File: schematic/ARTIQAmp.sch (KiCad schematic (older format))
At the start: 9 parts, among them J1 Power conneciton, J2 HD68, J3 HD68

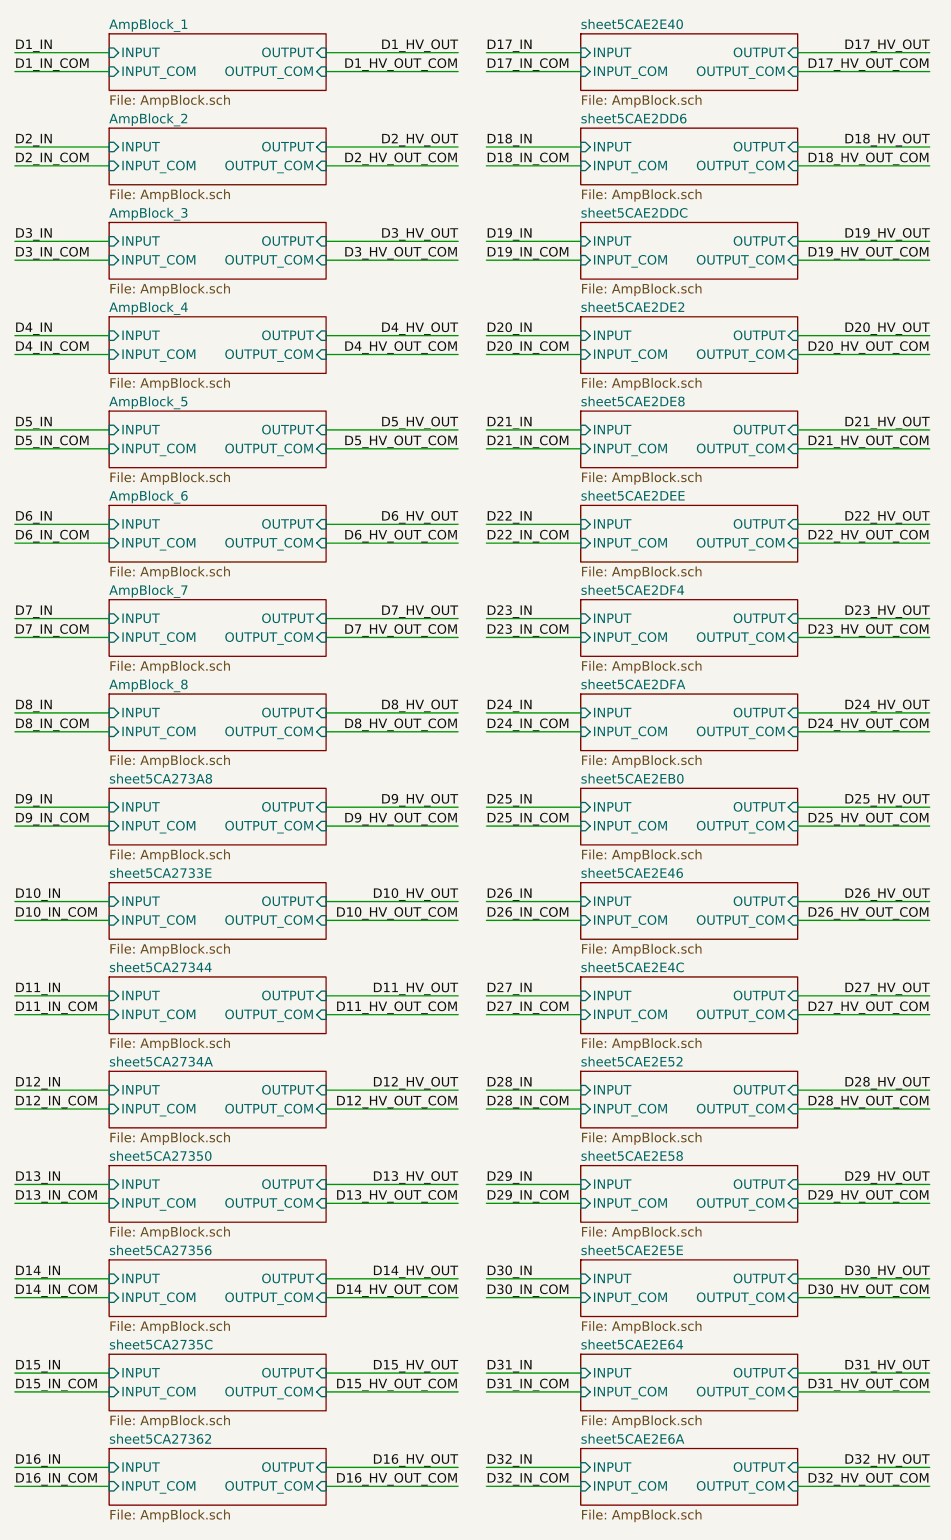
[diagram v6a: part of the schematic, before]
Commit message: Updating with recent changes as layout work starts
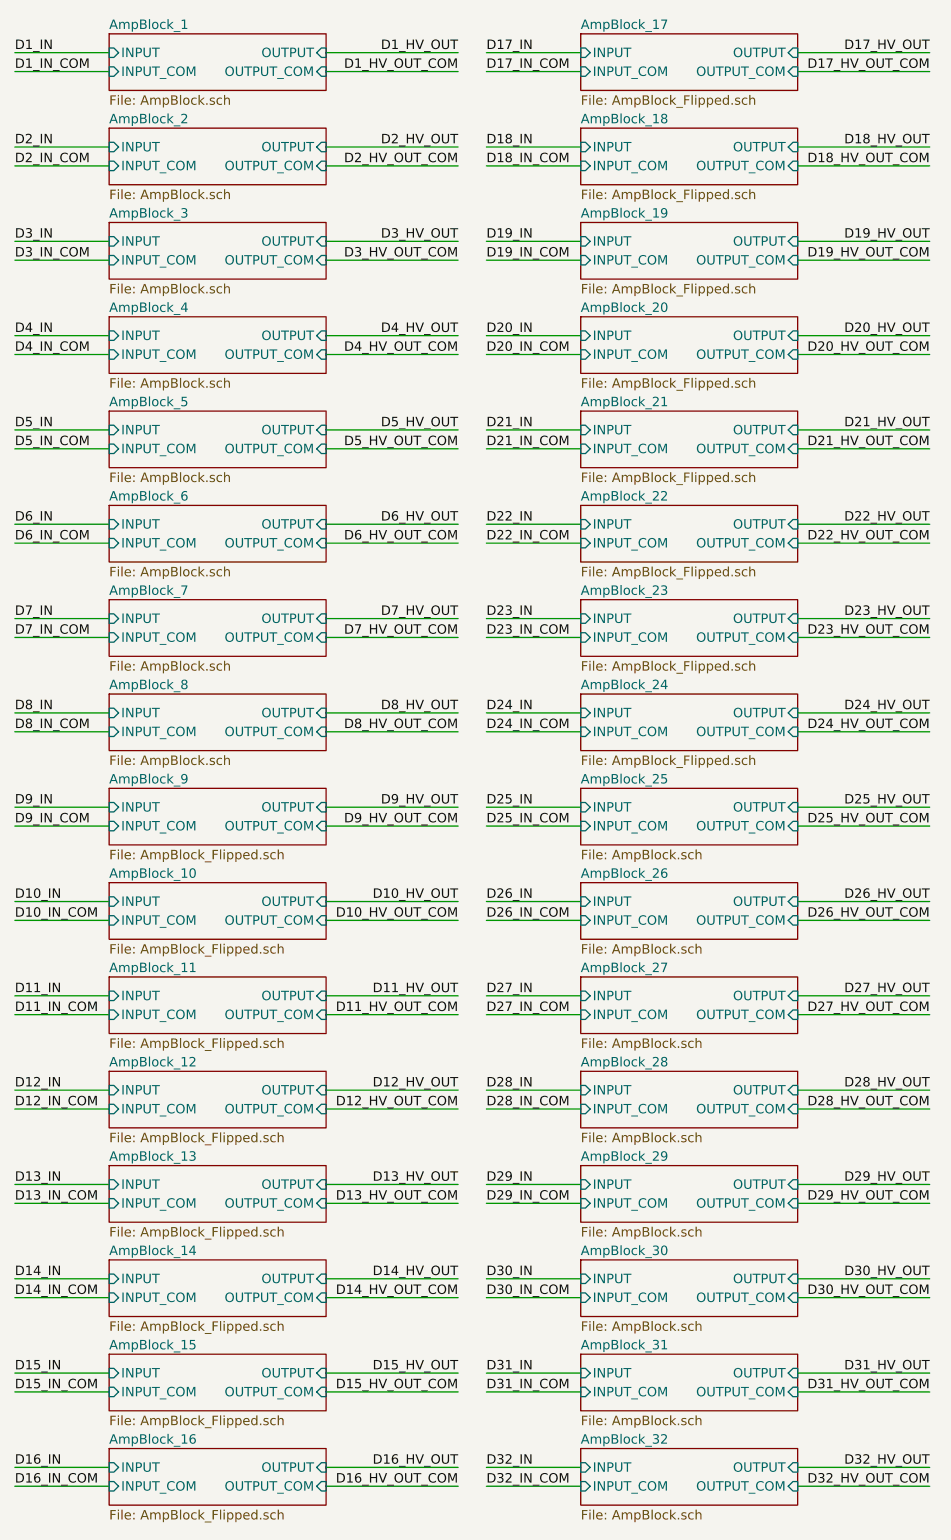
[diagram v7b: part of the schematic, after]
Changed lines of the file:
@@
 S 1150 5400 1150 300
 U 5CA2733E
-F0 "sheet5CA2733E" 50
-F1 "AmpBlock.sch" 50
+F0 "AmpBlock_10" 50
+F1 "AmpBlock_Flipped.sch" 50
 F2 "INPUT" I L 1150 5500 50
 F3 "OUTPUT" I R 2300 5500 50
@@
 S 1150 5900 1150 300
 U 5CA27344
-F0 "sheet5CA27344" 50
-F1 "AmpBlock.sch" 50
+F0 "AmpBlock_11" 50
+F1 "AmpBlock_Flipped.sch" 50
 F2 "INPUT" I L 1150 6000 50
 F3 "OUTPUT" I R 2300 6000 50
@@
 S 1150 6400 1150 300
 U 5CA2734A
-F0 "sheet5CA2734A" 50
-F1 "AmpBlock.sch" 50
+F0 "AmpBlock_12" 50
+F1 "AmpBlock_Flipped.sch" 50
 F2 "INPUT" I L 1150 6500 50
 F3 "OUTPUT" I R 2300 6500 50
@@
 S 1150 6900 1150 300
 U 5CA27350
-F0 "sheet5CA27350" 50
-F1 "AmpBlock.sch" 50
+F0 "AmpBlock_13" 50
+F1 "AmpBlock_Flipped.sch" 50
 F2 "INPUT" I L 1150 7000 50
 F3 "OUTPUT" I R 2300 7000 50
@@
 S 1150 7400 1150 300
 U 5CA27356
-F0 "sheet5CA27356" 50
-F1 "AmpBlock.sch" 50
+F0 "AmpBlock_14" 50
+F1 "AmpBlock_Flipped.sch" 50
 F2 "INPUT" I L 1150 7500 50
 F3 "OUTPUT" I R 2300 7500 50
@@
 S 1150 7900 1150 300
 U 5CA2735C
-F0 "sheet5CA2735C" 50
-F1 "AmpBlock.sch" 50
+F0 "AmpBlock_15" 50
+F1 "AmpBlock_Flipped.sch" 50
 F2 "INPUT" I L 1150 8000 50
 F3 "OUTPUT" I R 2300 8000 50
@@
 S 1150 8400 1150 300
 U 5CA27362
-F0 "sheet5CA27362" 50
-F1 "AmpBlock.sch" 50
+F0 "AmpBlock_16" 50
+F1 "AmpBlock_Flipped.sch" 50
 F2 "INPUT" I L 1150 8500 50
 F3 "OUTPUT" I R 2300 8500 50
@@
 S 1150 4900 1150 300
 U 5CA273A8
-F0 "sheet5CA273A8" 50
-F1 "AmpBlock.sch" 50
+F0 "AmpBlock_9" 50
+F1 "AmpBlock_Flipped.sch" 50
 F2 "INPUT" I L 1150 5000 50
 F3 "OUTPUT" I R 2300 5000 50
@@
 S 3650 1400 1150 300
 U 5CAE2DD6
-F0 "sheet5CAE2DD6" 50
-F1 "AmpBlock.sch" 50
+F0 "AmpBlock_18" 50
+F1 "AmpBlock_Flipped.sch" 50
 F2 "INPUT" I L 3650 1500 50
 F3 "OUTPUT" I R 4800 1500 50
@@
 S 3650 1900 1150 300
 U 5CAE2DDC
-F0 "sheet5CAE2DDC" 50
-F1 "AmpBlock.sch" 50
+F0 "AmpBlock_19" 50
+F1 "AmpBlock_Flipped.sch" 50
 F2 "INPUT" I L 3650 2000 50
 F3 "OUTPUT" I R 4800 2000 50
@@
 S 3650 2400 1150 300
 U 5CAE2DE2
-F0 "sheet5CAE2DE2" 50
-F1 "AmpBlock.sch" 50
+F0 "AmpBlock_20" 50
+F1 "AmpBlock_Flipped.sch" 50
 F2 "INPUT" I L 3650 2500 50
 F3 "OUTPUT" I R 4800 2500 50
@@
 S 3650 2900 1150 300
 U 5CAE2DE8
-F0 "sheet5CAE2DE8" 50
-F1 "AmpBlock.sch" 50
+F0 "AmpBlock_21" 50
+F1 "AmpBlock_Flipped.sch" 50
 F2 "INPUT" I L 3650 3000 50
 F3 "OUTPUT" I R 4800 3000 50
@@
 S 3650 3400 1150 300
 U 5CAE2DEE
-F0 "sheet5CAE2DEE" 50
-F1 "AmpBlock.sch" 50
+F0 "AmpBlock_22" 50
+F1 "AmpBlock_Flipped.sch" 50
 F2 "INPUT" I L 3650 3500 50
 F3 "OUTPUT" I R 4800 3500 50
@@
 S 3650 3900 1150 300
 U 5CAE2DF4
-F0 "sheet5CAE2DF4" 50
-F1 "AmpBlock.sch" 50
+F0 "AmpBlock_23" 50
+F1 "AmpBlock_Flipped.sch" 50
 F2 "INPUT" I L 3650 4000 50
 F3 "OUTPUT" I R 4800 4000 50
@@
 S 3650 4400 1150 300
 U 5CAE2DFA
-F0 "sheet5CAE2DFA" 50
-F1 "AmpBlock.sch" 50
+F0 "AmpBlock_24" 50
+F1 "AmpBlock_Flipped.sch" 50
 F2 "INPUT" I L 3650 4500 50
 F3 "OUTPUT" I R 4800 4500 50
@@
 S 3650 900  1150 300
 U 5CAE2E40
-F0 "sheet5CAE2E40" 50
-F1 "AmpBlock.sch" 50
+F0 "AmpBlock_17" 50
+F1 "AmpBlock_Flipped.sch" 50
 F2 "INPUT" I L 3650 1000 50
 F3 "OUTPUT" I R 4800 1000 50
@@
 S 3650 5400 1150 300
 U 5CAE2E46
-F0 "sheet5CAE2E46" 50
+F0 "AmpBlock_26" 50
 F1 "AmpBlock.sch" 50
 F2 "INPUT" I L 3650 5500 50
@@
 S 3650 5900 1150 300
 U 5CAE2E4C
-F0 "sheet5CAE2E4C" 50
+F0 "AmpBlock_27" 50
 F1 "AmpBlock.sch" 50
 F2 "INPUT" I L 3650 6000 50
@@
 $EndSheet
 $Sheet
-S 3650 6400 1150 300
-U 5CAE2E52
-F0 "sheet5CAE2E52" 50
-F1 "AmpBlock.sch" 50
-F2 "INPUT" I L 3650 6500 50
-F3 "OUTPUT" I R 4800 6500 50
-F4 "INPUT_COM" I L 3650 6600 50
-F5 "OUTPUT_COM" I R 4800 6600 50
-$EndSheet
-$Sheet
 S 3650 6900 1150 300
 U 5CAE2E58
-F0 "sheet5CAE2E58" 50
+F0 "AmpBlock_29" 50
 F1 "AmpBlock.sch" 50
 F2 "INPUT" I L 3650 7000 50
@@
 S 3650 7400 1150 300
 U 5CAE2E5E
-F0 "sheet5CAE2E5E" 50
+F0 "AmpBlock_30" 50
 F1 "AmpBlock.sch" 50
 F2 "INPUT" I L 3650 7500 50
@@
 S 3650 7900 1150 300
 U 5CAE2E64
-F0 "sheet5CAE2E64" 50
+F0 "AmpBlock_31" 50
 F1 "AmpBlock.sch" 50
 F2 "INPUT" I L 3650 8000 50
@@
 S 3650 8400 1150 300
 U 5CAE2E6A
-F0 "sheet5CAE2E6A" 50
+F0 "AmpBlock_32" 50
 F1 "AmpBlock.sch" 50
 F2 "INPUT" I L 3650 8500 50
@@
 Text Label 5500 8600 2    50   ~ 0
 D32_HV_OUT_COM
-$Sheet
-S 3650 4900 1150 300
-U 5CAE2EB0
-F0 "sheet5CAE2EB0" 50
-F1 "AmpBlock.sch" 50
-F2 "INPUT" I L 3650 5000 50
-F3 "OUTPUT" I R 4800 5000 50
-F4 "INPUT_COM" I L 3650 5100 50
-F5 "OUTPUT_COM" I R 4800 5100 50
-$EndSheet
 Text Label 12750 6550 2    50   ~ 0
 D32_HV_OUT_COM
@@
 	10650 2150 10250 2150
 Connection ~ 10250 2150
+$Sheet
+S 3650 4900 1150 300
+U 5CAE2EB0
+F0 "AmpBlock_25" 50
+F1 "AmpBlock.sch" 50
+F2 "INPUT" I L 3650 5000 50
+F3 "OUTPUT" I R 4800 5000 50
+F4 "INPUT_COM" I L 3650 5100 50
+F5 "OUTPUT_COM" I R 4800 5100 50
+$EndSheet
+$Sheet
+S 3650 6400 1150 300
+U 5CAE2E52
+F0 "AmpBlock_28" 50
+F1 "AmpBlock.sch" 50
+F2 "INPUT" I L 3650 6500 50
+F3 "OUTPUT" I R 4800 6500 50
+F4 "INPUT_COM" I L 3650 6600 50
+F5 "OUTPUT_COM" I R 4800 6600 50
+$EndSheet
 $EndSCHEMATC

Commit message: Complete initial layout and swap components around in schematic
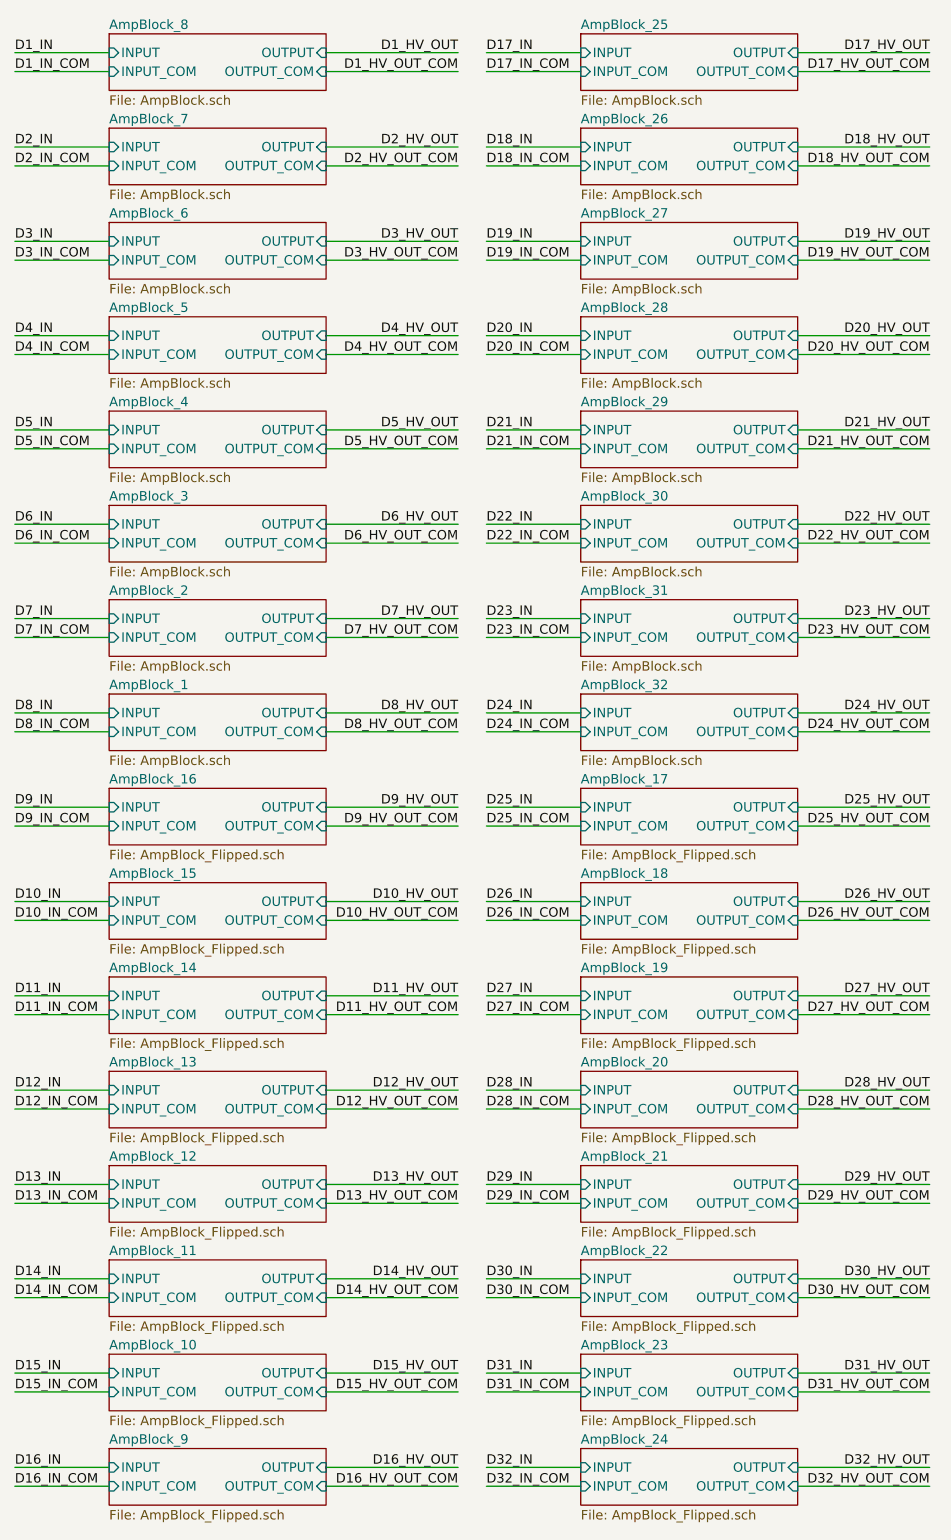
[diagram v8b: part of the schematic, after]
